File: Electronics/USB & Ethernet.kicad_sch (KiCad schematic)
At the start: 13 parts

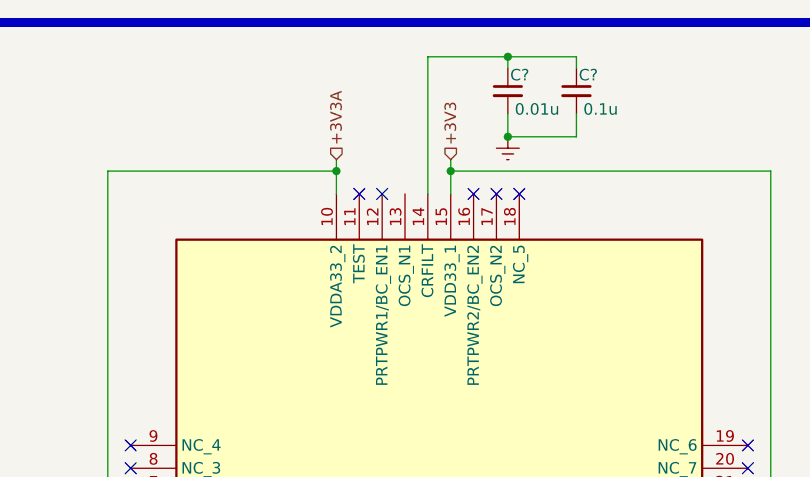
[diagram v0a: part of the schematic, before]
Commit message: RP2040 Added, Files Structure Changed
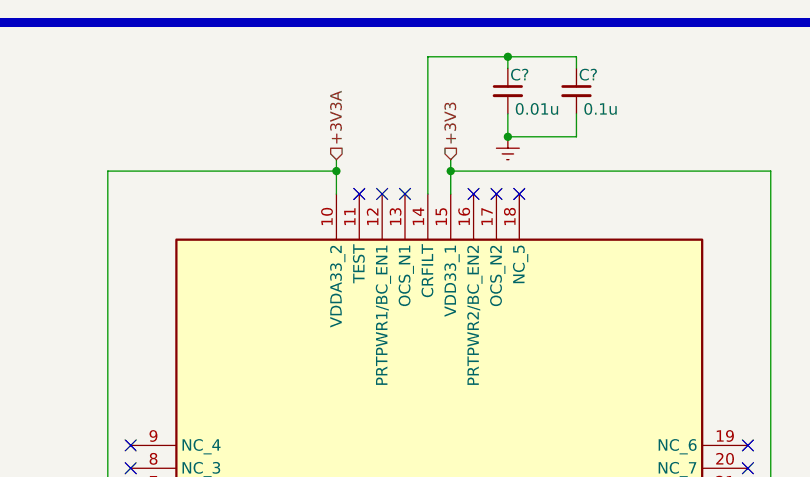
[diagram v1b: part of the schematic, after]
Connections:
- no-connect marks 16 -> 17
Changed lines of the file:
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@@
+	)
+	(no_connect
+		(at 146.05 36.83)
 	)
 	(no_connect

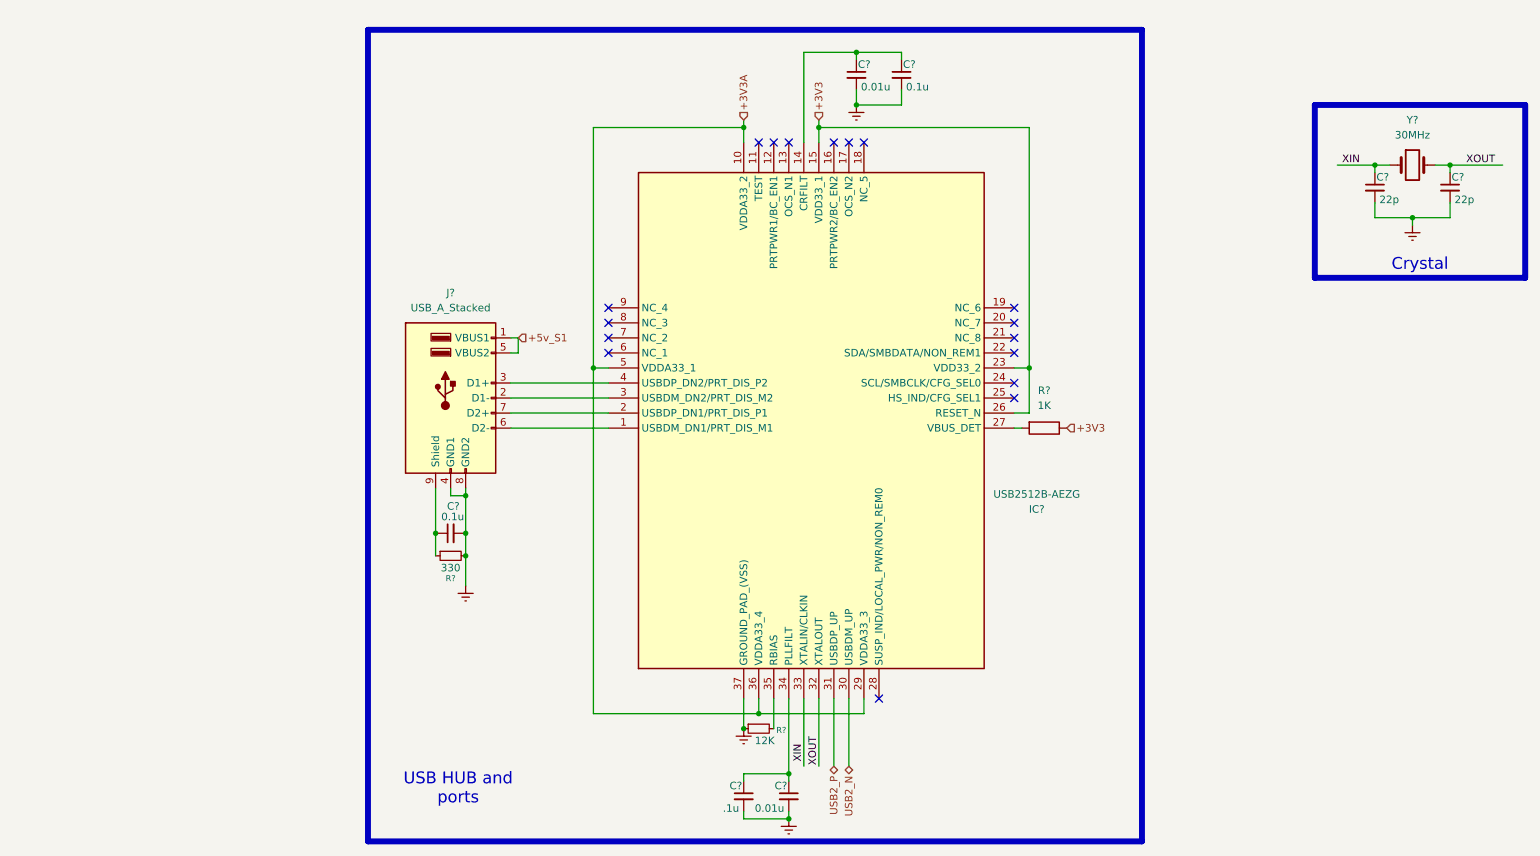
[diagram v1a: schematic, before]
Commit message: Rp2040 Power Sequence finished and general cleaning
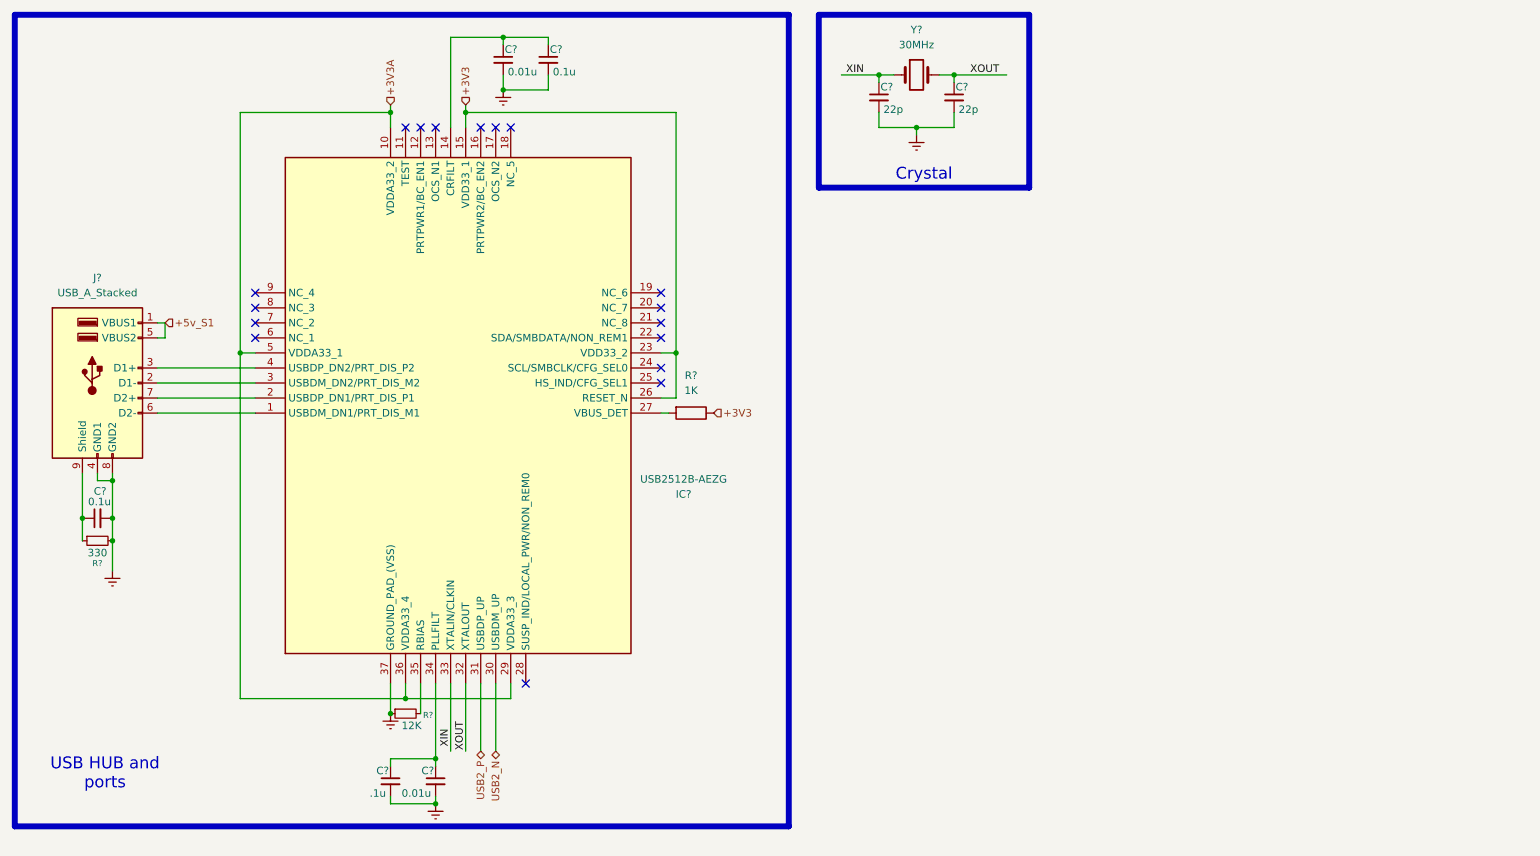
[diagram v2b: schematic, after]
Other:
- moved on the sheet: C?, IC?, J?, R?, Y?

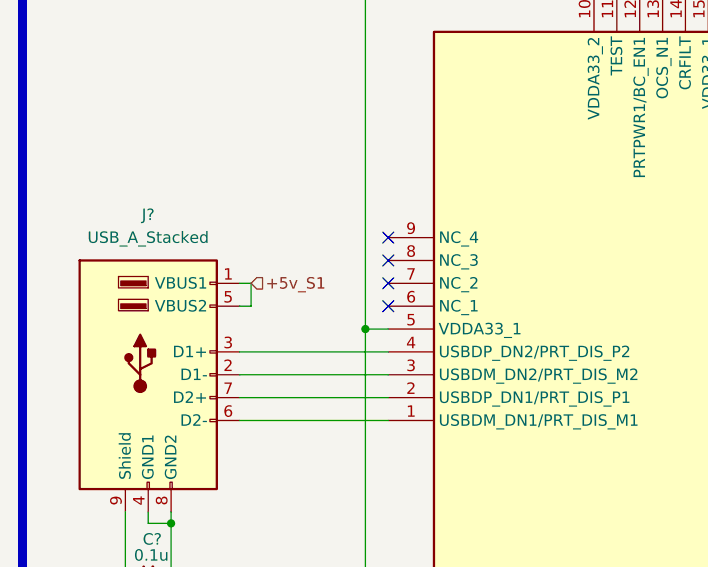
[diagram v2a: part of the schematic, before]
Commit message: Starting the Sheet connections
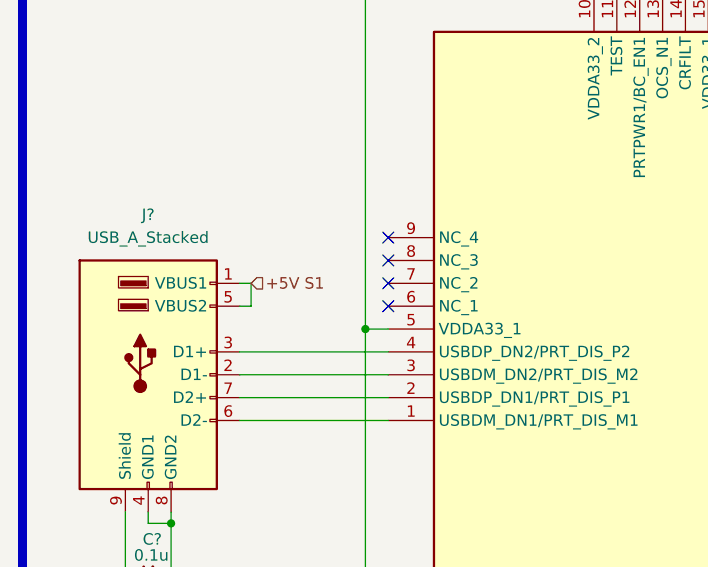
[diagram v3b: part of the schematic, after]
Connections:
- net +5v_S1 renamed +5V S1
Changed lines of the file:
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@@
 		)
 	)
-	(hierarchical_label "+5v_S1"
+	(hierarchical_label "+5V S1"
 		(shape input)
 		(at 40.64 67.31 0)

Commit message: Footprints Selected
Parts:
- removed C? (x2): 22p, symbol Device:C_Small
- removed Y?: 30MHz, symbol Device:Crystal
- added C152, C153: 22p, Capacitor_SMD:C_0603_1608Metric, symbol Device:C_Small
- added Y3: 30MHz, ABM8-30.000MHZ-B2-T:ABM810000MHZ12D2W, symbol Device:Crystal_GND24
- C147, C148, C149, C150, C151: renamed from C?; footprint (none) -> Capacitor_SMD:C_0603_1608Metric
- IC4: renamed from IC?; footprint QFN50P600X600X100-37N-D -> USB2512B-AEZG:QFN50P600X600X100-37N-D
- J24: renamed from J?; footprint (none) -> Connector_USB:USB_A_Wuerth_61400826021_Horizontal_Stacked
- R86, R87, R88: renamed from R?; footprint (none) -> Resistor_SMD:R_0603_1608Metric
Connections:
- net XIN: now also C152.1, Y3.1
- net XOUT: now also C153.1, Y3.3
- new net: C152.2, C153.2, Y3.4

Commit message: Footprints selected, Hiracicle connections created, Pcb next
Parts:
- C147: renamed from C150; value 0.01u -> 0u01; footprint Capacitor_SMD:C_0603_1608Metric -> Capacitor_SMD:C_0402_1005Metric
- C148: renamed from C151; value 0.1u -> 100n
- C149: renamed from C152; footprint Capacitor_SMD:C_0603_1608Metric -> Capacitor_SMD:C_0402_1005Metric
- C150: renamed from C153; footprint Capacitor_SMD:C_0603_1608Metric -> Capacitor_SMD:C_0402_1005Metric
- C151: renamed from C147; value 0.1u -> 100n
- C152: renamed from C148; value .1u -> 100n
- C153: renamed from C149; value 0.01u -> 0u01; footprint Capacitor_SMD:C_0603_1608Metric -> Capacitor_SMD:C_0402_1005Metric
- renumbered R88 to R84, R86 to R85, R87 to R86
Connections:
- net gnd: now reaches IC4.37 (GROUND_PAD_(VSS)), R86.1
- net gnd: now also C147.2, C148.2, C149.2, C150.2, C151.2, C152.2, C153.2, J24.4 (GND1), J24.8 (GND2), R85.2, Y3.2, Y3.4
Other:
- moved on the sheet: R86
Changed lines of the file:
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@@
 	(text_box "USB HUB and ports\n"
 		(exclude_from_sim no)
-		(at 16.51 138.43 0)
+		(at 16.51 140.97 0)
 		(size 27.94 9.525)
 		(margins 1.9049 1.9049 1.9049 1.9049)
@@
 	)
 	(junction
-		(at 78.74 133.35)
+		(at 78.74 134.62)
 		(diameter 0)
 		(color 0 0 0 0)
@@
 	(wire
 		(pts
-			(xy 83.82 128.27) (xy 83.82 133.35)
+			(xy 83.82 128.27) (xy 83.82 134.62)
 		)
 		(stroke
@@
 	(wire
 		(pts
+			(xy 78.74 128.27) (xy 78.74 134.62)
+		)
+		(stroke
+			(width 0)
+			(type default)
+		)
+	)
+	(wire
+		(pts
 			(xy 78.74 147.32) (xy 78.74 148.59)
 		)
@@
 		(pts
 			(xy 39.37 77.47) (xy 55.88 77.47)
-		)
-		(stroke
-			(width 0)
-			(type default)
-		)
-	)
-	(wire
-		(pts
-			(xy 78.74 128.27) (xy 78.74 133.35)
 		)
 		(stroke
@@
 		(on_board yes)
 		(dnp no)
-		(property "Reference" "#PWR0169"
+		(property "Reference" "#PWR0167"
 			(at 97.79 34.29 0)
 			(effects
@@
 			)
 		)
-		(property "Value" "~"
+		(property "Value" "gnd"
 			(at 97.79 31.75 0)
 			(effects
@@
 			(project "CM5 Nas"
 				(path "/0650c7a8-acba-429c-9f8e-eec0baf0bc1c/fede4c36-00cc-4d3d-b71c-5243ba232202/6a9d58eb-7efc-489b-8392-0909cd6b0d5f"
-					(reference "#PWR0169")
+					(reference "#PWR0167")
 					(unit 1)
 				)
@@
 		(on_board yes)
 		(dnp no)
-		(property "Reference" "C149"
+		(property "Reference" "C153"
 			(at 86.106 143.002 0)
 			(effects
@@
 			)
 		)
-		(property "Value" "0.01u"
+		(property "Value" "0u01"
 			(at 85.598 146.812 0)
 			(effects
@@
 			)
 		)
-		(property "Footprint" "Capacitor_SMD:C_0603_1608Metric"
+		(property "Footprint" "Capacitor_SMD:C_0402_1005Metric"
 			(at 86.36 144.78 0)
 			(effects
@@
 			(project "CM5 Nas"
 				(path "/0650c7a8-acba-429c-9f8e-eec0baf0bc1c/fede4c36-00cc-4d3d-b71c-5243ba232202/6a9d58eb-7efc-489b-8392-0909cd6b0d5f"
-					(reference "C149")
+					(reference "C153")
 					(unit 1)
 				)
@@
 		(on_board yes)
 		(dnp no)
-		(property "Reference" "C148"
+		(property "Reference" "C152"
 			(at 78.486 143.002 0)
 			(effects
@@
 			)
 		)
-		(property "Value" ".1u"
+		(property "Value" "100n"
 			(at 77.978 146.812 0)
 			(effects
@@
 			(project "CM5 Nas"
 				(path "/0650c7a8-acba-429c-9f8e-eec0baf0bc1c/fede4c36-00cc-4d3d-b71c-5243ba232202/6a9d58eb-7efc-489b-8392-0909cd6b0d5f"
-					(reference "C148")
+					(reference "C152")
 					(unit 1)
 				)
@@
 		(on_board yes)
 		(dnp no)
-		(property "Reference" "R86"
+		(property "Reference" "R85"
 			(at 29.21 107.95 90)
 			(effects
@@
 			(project "CM5 Nas"
 				(path "/0650c7a8-acba-429c-9f8e-eec0baf0bc1c/fede4c36-00cc-4d3d-b71c-5243ba232202/6a9d58eb-7efc-489b-8392-0909cd6b0d5f"
-					(reference "R86")
+					(reference "R85")
 					(unit 1)
 				)
@@
 		(on_board yes)
 		(dnp no)
-		(property "Reference" "C153"
+		(property "Reference" "C150"
 			(at 172.974 26.162 0)
 			(effects
@@
 			)
 		)
-		(property "Footprint" "Capacitor_SMD:C_0603_1608Metric"
+		(property "Footprint" "Capacitor_SMD:C_0402_1005Metric"
 			(at 172.72 27.94 0)
 			(effects
@@
 			(project "CM5 Nas"
 				(path "/0650c7a8-acba-429c-9f8e-eec0baf0bc1c/fede4c36-00cc-4d3d-b71c-5243ba232202/6a9d58eb-7efc-489b-8392-0909cd6b0d5f"
-					(reference "C153")
+					(reference "C150")
 					(unit 1)
 				)
@@
 		(on_board yes)
 		(dnp no)
-		(property "Reference" "C150"
+		(property "Reference" "C147"
 			(at 98.044 21.082 0)
 			(effects
@@
 			)
 		)
-		(property "Value" "0.01u"
+		(property "Value" "0u01"
 			(at 98.552 24.892 0)
 			(effects
@@
 			)
 		)
-		(property "Footprint" "Capacitor_SMD:C_0603_1608Metric"
+		(property "Footprint" "Capacitor_SMD:C_0402_1005Metric"
 			(at 97.79 22.86 0)
 			(effects
@@
 			(project "CM5 Nas"
 				(path "/0650c7a8-acba-429c-9f8e-eec0baf0bc1c/fede4c36-00cc-4d3d-b71c-5243ba232202/6a9d58eb-7efc-489b-8392-0909cd6b0d5f"
-					(reference "C150")
+					(reference "C147")
 					(unit 1)
 				)
@@
 		(on_board yes)
 		(dnp no)
-		(property "Reference" "#PWR0170"
+		(property "Reference" "#PWR0166"
 			(at 162.56 25.4 0)
 			(effects
@@
 			)
 		)
-		(property "Value" "~"
+		(property "Value" "gnd"
 			(at 162.56 22.86 0)
 			(effects
@@
 			(project "CM5 Nas"
 				(path "/0650c7a8-acba-429c-9f8e-eec0baf0bc1c/fede4c36-00cc-4d3d-b71c-5243ba232202/6a9d58eb-7efc-489b-8392-0909cd6b0d5f"
-					(reference "#PWR0170")
+					(reference "#PWR0166")
 					(unit 1)
 				)
@@
 		(on_board yes)
 		(dnp no)
-		(property "Reference" "#PWR0171"
+		(property "Reference" "#PWR0168"
 			(at 166.37 40.64 0)
 			(effects
@@
 			)
 		)
-		(property "Value" "~"
+		(property "Value" "gnd"
 			(at 166.37 38.1 0)
 			(effects
@@
 			(project "CM5 Nas"
 				(path "/0650c7a8-acba-429c-9f8e-eec0baf0bc1c/fede4c36-00cc-4d3d-b71c-5243ba232202/6a9d58eb-7efc-489b-8392-0909cd6b0d5f"
-					(reference "#PWR0171")
+					(reference "#PWR0168")
 					(unit 1)
 				)
@@
 		(on_board yes)
 		(dnp no)
-		(property "Reference" "#PWR0168"
+		(property "Reference" "#PWR0171"
 			(at 86.36 154.94 0)
 			(effects
@@
 			)
 		)
-		(property "Value" "~"
+		(property "Value" "gnd"
 			(at 86.36 152.4 0)
 			(effects
@@
 			(project "CM5 Nas"
 				(path "/0650c7a8-acba-429c-9f8e-eec0baf0bc1c/fede4c36-00cc-4d3d-b71c-5243ba232202/6a9d58eb-7efc-489b-8392-0909cd6b0d5f"
-					(reference "#PWR0168")
+					(reference "#PWR0171")
 					(unit 1)
 				)
@@
 		(on_board yes)
 		(dnp no)
-		(property "Reference" "C151"
+		(property "Reference" "C148"
 			(at 105.664 21.082 0)
 			(effects
@@
 			)
 		)
-		(property "Value" "0.1u"
+		(property "Value" "100n"
 			(at 106.172 24.892 0)
 			(effects
@@
 			(project "CM5 Nas"
 				(path "/0650c7a8-acba-429c-9f8e-eec0baf0bc1c/fede4c36-00cc-4d3d-b71c-5243ba232202/6a9d58eb-7efc-489b-8392-0909cd6b0d5f"
-					(reference "C151")
+					(reference "C148")
 					(unit 1)
 				)
@@
 	(symbol
 		(lib_id "Device:R_Small")
-		(at 81.28 133.35 90)
+		(at 81.28 134.62 90)
 		(mirror x)
 		(unit 1)
@@
 		(on_board yes)
 		(dnp no)
-		(property "Reference" "R87"
-			(at 85.09 133.604 90)
+		(property "Reference" "R86"
+			(at 81.28 133.096 90)
 			(effects
 				(font
@@
 		)
 		(property "Value" "12K"
-			(at 82.296 135.382 90)
+			(at 82.296 136.652 90)
 			(effects
 				(font
@@
 		)
 		(property "Footprint" "Resistor_SMD:R_0603_1608Metric"
-			(at 81.28 133.35 0)
+			(at 81.28 134.62 0)
 			(effects
 				(font
@@
 		)
 		(property "Datasheet" "~"
-			(at 81.28 133.35 0)
+			(at 81.28 134.62 0)
 			(effects
 				(font
@@
 		)
 		(property "Description" "Resistor, small symbol"
-			(at 81.28 133.35 0)
+			(at 81.28 134.62 0)
 			(effects
 				(font
@@
 			(project ""
 				(path "/0650c7a8-acba-429c-9f8e-eec0baf0bc1c/fede4c36-00cc-4d3d-b71c-5243ba232202/6a9d58eb-7efc-489b-8392-0909cd6b0d5f"
-					(reference "R87")
+					(reference "R86")
 					(unit 1)
 				)
@@
 		(on_board yes)
 		(dnp no)
-		(property "Reference" "#PWR0166"
+		(property "Reference" "#PWR0169"
 			(at 31.75 115.57 0)
 			(effects
@@
 			)
 		)
-		(property "Value" "~"
+		(property "Value" "gnd"
 			(at 31.75 113.03 0)
 			(effects
@@
 			(project "CM5 Nas"
 				(path "/0650c7a8-acba-429c-9f8e-eec0baf0bc1c/fede4c36-00cc-4d3d-b71c-5243ba232202/6a9d58eb-7efc-489b-8392-0909cd6b0d5f"
-					(reference "#PWR0166")
+					(reference "#PWR0169")
 					(unit 1)
 				)
@@
 	(symbol
 		(lib_id "power:Earth")
-		(at 78.74 133.35 0)
+		(at 78.74 134.62 0)
 		(unit 1)
 		(exclude_from_sim no)
@@
 		(on_board yes)
 		(dnp no)
-		(property "Reference" "#PWR0167"
-			(at 78.74 139.7 0)
-			(effects
-				(font
-					(size 1.27 1.27)
-				)
-				(hide yes)
-			)
-		)
-		(property "Value" "~"
-			(at 78.74 137.16 0)
+		(property "Reference" "#PWR0170"
+			(at 78.74 140.97 0)
+			(effects
+				(font
+					(size 1.27 1.27)
+				)
+				(hide yes)
+			)
+		)
+		(property "Value" "gnd"
+			(at 78.74 138.43 0)
 			(effects
 				(font
@@
 		)
 		(property "Footprint" ""
-			(at 78.74 133.35 0)
+			(at 78.74 134.62 0)
 			(effects
 				(font
@@
 		)
 		(property "Datasheet" "~"
-			(at 78.74 133.35 0)
+			(at 78.74 134.62 0)
 			(effects
 				(font
@@
 		)
 		(property "Description" "Power symbol creates a global label with name \"Earth\""
-			(at 78.74 133.35 0)
+			(at 78.74 134.62 0)
 			(effects
 				(font
@@
 			(project "CM5 Nas"
 				(path "/0650c7a8-acba-429c-9f8e-eec0baf0bc1c/fede4c36-00cc-4d3d-b71c-5243ba232202/6a9d58eb-7efc-489b-8392-0909cd6b0d5f"
-					(reference "#PWR0167")
+					(reference "#PWR0170")
 					(unit 1)
 				)
@@
 		(dnp no)
 		(fields_autoplaced yes)
-		(property "Reference" "R88"
+		(property "Reference" "R84"
 			(at 129.54 76.2 90)
 			(effects
@@
 			(project ""
 				(path "/0650c7a8-acba-429c-9f8e-eec0baf0bc1c/fede4c36-00cc-4d3d-b71c-5243ba232202/6a9d58eb-7efc-489b-8392-0909cd6b0d5f"
-					(reference "R88")
+					(reference "R84")
 					(unit 1)
 				)
@@
 		(on_board yes)
 		(dnp no)
-		(property "Reference" "C147"
+		(property "Reference" "C151"
 			(at 30.734 95.758 90)
 			(effects
@@
 			)
 		)
-		(property "Value" "0.1u"
+		(property "Value" "100n"
 			(at 31.496 97.536 90)
 			(effects
@@
 			(project "CM5 Nas"
 				(path "/0650c7a8-acba-429c-9f8e-eec0baf0bc1c/fede4c36-00cc-4d3d-b71c-5243ba232202/6a9d58eb-7efc-489b-8392-0909cd6b0d5f"
-					(reference "C147")
+					(reference "C151")
 					(unit 1)
 				)
@@
 		(on_board yes)
 		(dnp no)
-		(property "Reference" "C152"
+		(property "Reference" "C149"
 			(at 159.766 26.162 0)
 			(effects
@@
 			)
 		)
-		(property "Footprint" "Capacitor_SMD:C_0603_1608Metric"
+		(property "Footprint" "Capacitor_SMD:C_0402_1005Metric"
 			(at 160.02 27.94 0)
 			(effects
@@
 			(project "CM5 Nas"
 				(path "/0650c7a8-acba-429c-9f8e-eec0baf0bc1c/fede4c36-00cc-4d3d-b71c-5243ba232202/6a9d58eb-7efc-489b-8392-0909cd6b0d5f"
-					(reference "C152")
+					(reference "C149")
 					(unit 1)
 				)
